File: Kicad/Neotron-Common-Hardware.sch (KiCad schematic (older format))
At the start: 17 parts, among them J101 Neotron-Expansion-Slot, J102 Neotron-Expansion-Slot, J103 Neotron-Expansion-Slot, J104 Neotron-Expansion-Slot, U101 Neotron-CPU

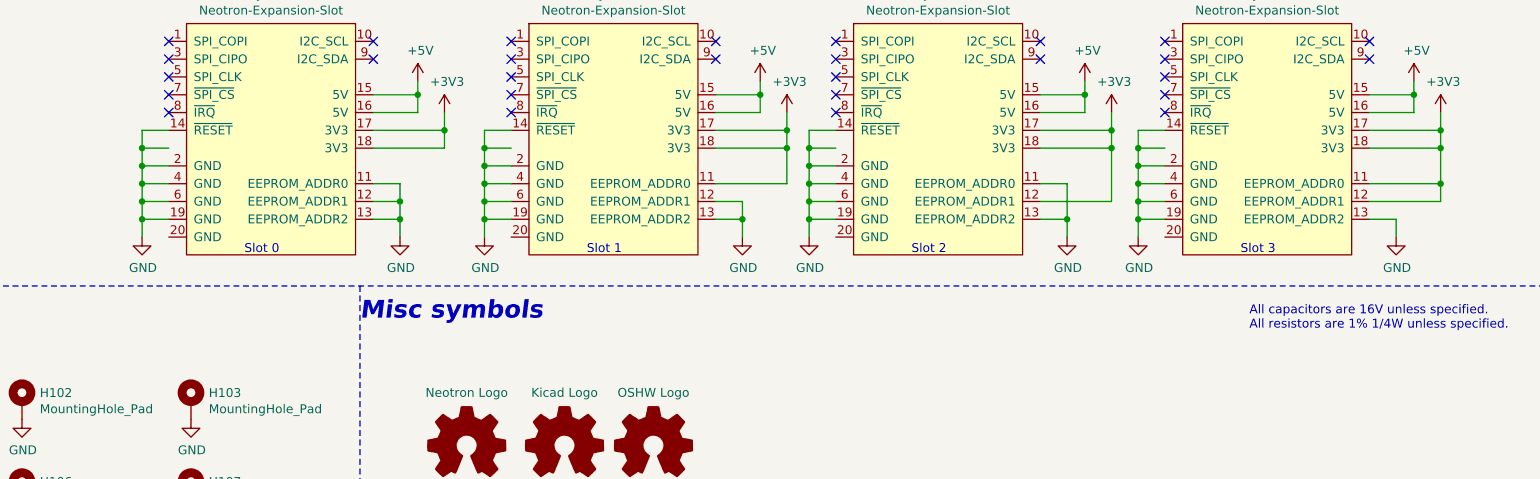
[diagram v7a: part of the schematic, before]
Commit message: Rejigged expansion socket, and added pinout to README.
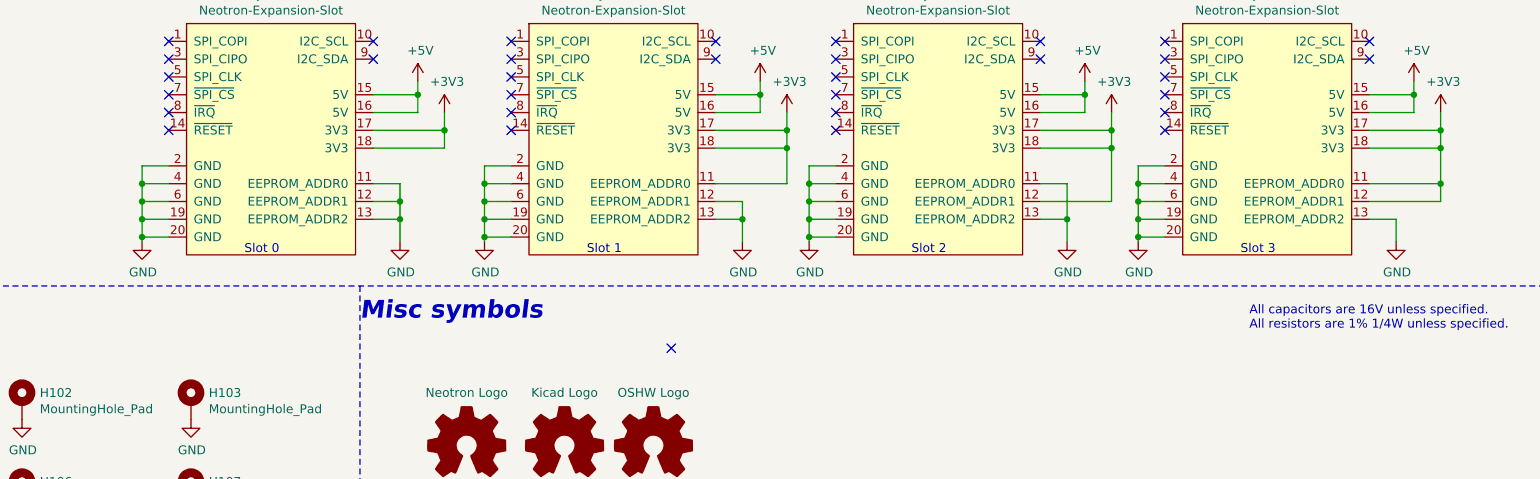
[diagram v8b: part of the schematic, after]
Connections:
- wire segments 128 -> 120
- no-connect marks 120 -> 125
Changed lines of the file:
@@
 L power:GND #PWR0118
 U 1 1 5FED032B
-P 3225 5475
-F 0 "#PWR0118" H 3225 5225 50  0001 C CNN
-F 1 "GND" H 3230 5302 50  0000 C CNN
-F 2 "" H 3225 5475 50  0001 C CNN
-F 3 "" H 3225 5475 50  0001 C CNN
-	1    3225 5475
-	1    0    0    -1
-$EndComp
-Wire Wire Line
-	3375 4875 3225 4875
-Wire Wire Line
-	3375 4975 3225 4975
-Wire Wire Line
-	3225 4875 3225 4975
-Connection ~ 3225 4975
-Wire Wire Line
-	3225 4975 3225 5075
+P 3225 5500
+F 0 "#PWR0118" H 3225 5250 50  0001 C CNN
+F 1 "GND" H 3230 5327 50  0000 C CNN
+F 2 "" H 3225 5500 50  0001 C CNN
+F 3 "" H 3225 5500 50  0001 C CNN
+	1    3225 5500
+	1    0    0    -1
+$EndComp
 Wire Wire Line
 	3375 5075 3225 5075
-Connection ~ 3225 5075
 Wire Wire Line
 	3225 5075 3225 5175
@@
 L power:GND #PWR0119
 U 1 1 5FED378B
-P 4675 5475
-F 0 "#PWR0119" H 4675 5225 50  0001 C CNN
-F 1 "GND" H 4680 5302 50  0000 C CNN
-F 2 "" H 4675 5475 50  0001 C CNN
-F 3 "" H 4675 5475 50  0001 C CNN
-	1    4675 5475
+P 4675 5500
+F 0 "#PWR0119" H 4675 5250 50  0001 C CNN
+F 1 "GND" H 4680 5327 50  0000 C CNN
+F 2 "" H 4675 5500 50  0001 C CNN
+F 3 "" H 4675 5500 50  0001 C CNN
+	1    4675 5500
 	1    0    0    -1
 $EndComp
@@
 	4525 5375 4675 5375
 Wire Wire Line
-	4675 5375 4675 5475
+	4675 5375 4675 5500
 Wire Wire Line
 	4525 5275 4675 5275
@@
 L power:GND #PWR0122
 U 1 1 5FEDE866
-P 5150 5475
-F 0 "#PWR0122" H 5150 5225 50  0001 C CNN
-F 1 "GND" H 5155 5302 50  0000 C CNN
-F 2 "" H 5150 5475 50  0001 C CNN
-F 3 "" H 5150 5475 50  0001 C CNN
-	1    5150 5475
-	1    0    0    -1
-$EndComp
-Wire Wire Line
-	5300 4875 5150 4875
-Wire Wire Line
-	5300 4975 5150 4975
-Wire Wire Line
-	5150 4875 5150 4975
-Connection ~ 5150 4975
-Wire Wire Line
-	5150 4975 5150 5075
+P 5150 5500
+F 0 "#PWR0122" H 5150 5250 50  0001 C CNN
+F 1 "GND" H 5155 5327 50  0000 C CNN
+F 2 "" H 5150 5500 50  0001 C CNN
+F 3 "" H 5150 5500 50  0001 C CNN
+	1    5150 5500
+	1    0    0    -1
+$EndComp
 Wire Wire Line
 	5300 5075 5150 5075
-Connection ~ 5150 5075
 Wire Wire Line
 	5150 5075 5150 5175
@@
 L power:GND #PWR0123
 U 1 1 5FEDE881
-P 6600 5475
-F 0 "#PWR0123" H 6600 5225 50  0001 C CNN
-F 1 "GND" H 6605 5302 50  0000 C CNN
-F 2 "" H 6600 5475 50  0001 C CNN
-F 3 "" H 6600 5475 50  0001 C CNN
-	1    6600 5475
+P 6600 5500
+F 0 "#PWR0123" H 6600 5250 50  0001 C CNN
+F 1 "GND" H 6605 5327 50  0000 C CNN
+F 2 "" H 6600 5500 50  0001 C CNN
+F 3 "" H 6600 5500 50  0001 C CNN
+	1    6600 5500
 	1    0    0    -1
 $EndComp
@@
 	6450 5375 6600 5375
 Wire Wire Line
-	6600 5375 6600 5475
+	6600 5375 6600 5500
 Wire Wire Line
 	6450 5275 6600 5275
@@
 L power:GND #PWR0126
 U 1 1 5FEED11A
-P 6975 5475
-F 0 "#PWR0126" H 6975 5225 50  0001 C CNN
-F 1 "GND" H 6980 5302 50  0000 C CNN
-F 2 "" H 6975 5475 50  0001 C CNN
-F 3 "" H 6975 5475 50  0001 C CNN
-	1    6975 5475
-	1    0    0    -1
-$EndComp
-Wire Wire Line
-	7125 4875 6975 4875
-Wire Wire Line
-	7125 4975 6975 4975
-Wire Wire Line
-	6975 4875 6975 4975
-Connection ~ 6975 4975
-Wire Wire Line
-	6975 4975 6975 5075
+P 6975 5500
+F 0 "#PWR0126" H 6975 5250 50  0001 C CNN
+F 1 "GND" H 6980 5327 50  0000 C CNN
+F 2 "" H 6975 5500 50  0001 C CNN
+F 3 "" H 6975 5500 50  0001 C CNN
+	1    6975 5500
+	1    0    0    -1
+$EndComp
 Wire Wire Line
 	7125 5075 6975 5075
-Connection ~ 6975 5075
 Wire Wire Line
 	6975 5075 6975 5175
@@
 L power:GND #PWR0129
 U 1 1 5FF20385
-P 8425 5475
-F 0 "#PWR0129" H 8425 5225 50  0001 C CNN
-F 1 "GND" H 8430 5302 50  0000 C CNN
-F 2 "" H 8425 5475 50  0001 C CNN
-F 3 "" H 8425 5475 50  0001 C CNN
-	1    8425 5475
+P 8425 5500
+F 0 "#PWR0129" H 8425 5250 50  0001 C CNN
+F 1 "GND" H 8430 5327 50  0000 C CNN
+F 2 "" H 8425 5500 50  0001 C CNN
+F 3 "" H 8425 5500 50  0001 C CNN
+	1    8425 5500
 	1    0    0    -1
 $EndComp
@@
 Connection ~ 8425 5375
 Wire Wire Line
-	8425 5375 8425 5475
+	8425 5375 8425 5500
 Wire Wire Line
 	8275 5275 8675 5275
@@
 L power:GND #PWR0130
 U 1 1 5FF3FC0D
-P 8825 5475
-F 0 "#PWR0130" H 8825 5225 50  0001 C CNN
-F 1 "GND" H 8830 5302 50  0000 C CNN
-F 2 "" H 8825 5475 50  0001 C CNN
-F 3 "" H 8825 5475 50  0001 C CNN
-	1    8825 5475
-	1    0    0    -1
-$EndComp
-Wire Wire Line
-	8975 4875 8825 4875
-Wire Wire Line
-	8975 4975 8825 4975
-Wire Wire Line
-	8825 4875 8825 4975
-Connection ~ 8825 4975
-Wire Wire Line
-	8825 4975 8825 5075
+P 8825 5500
+F 0 "#PWR0130" H 8825 5250 50  0001 C CNN
+F 1 "GND" H 8830 5327 50  0000 C CNN
+F 2 "" H 8825 5500 50  0001 C CNN
+F 3 "" H 8825 5500 50  0001 C CNN
+	1    8825 5500
+	1    0    0    -1
+$EndComp
 Wire Wire Line
 	8975 5075 8825 5075
-Connection ~ 8825 5075
 Wire Wire Line
 	8825 5075 8825 5175
@@
 L power:GND #PWR0133
 U 1 1 5FF3FC4F
-P 10275 5475
-F 0 "#PWR0133" H 10275 5225 50  0001 C CNN
-F 1 "GND" H 10280 5302 50  0000 C CNN
-F 2 "" H 10275 5475 50  0001 C CNN
-F 3 "" H 10275 5475 50  0001 C CNN
-	1    10275 5475
+P 10275 5500
+F 0 "#PWR0133" H 10275 5250 50  0001 C CNN
+F 1 "GND" H 10280 5327 50  0000 C CNN
+F 2 "" H 10275 5500 50  0001 C CNN
+F 3 "" H 10275 5500 50  0001 C CNN
+	1    10275 5500
 	1    0    0    -1
 $EndComp
@@
 	10125 5375 10275 5375
 Wire Wire Line
-	10275 5375 10275 5475
+	10275 5375 10275 5500
 Wire Wire Line
 	10125 5275 10525 5275
@@
 Wire Wire Line
 	10525 5175 10525 5275
+Wire Wire Line
+	3375 5475 3225 5475
+Connection ~ 3225 5475
+Wire Wire Line
+	3225 5475 3225 5500
+Wire Wire Line
+	5300 5475 5150 5475
+Connection ~ 5150 5475
+Wire Wire Line
+	5150 5475 5150 5500
+Wire Wire Line
+	8975 5475 8825 5475
+Connection ~ 8825 5475
+Wire Wire Line
+	8825 5475 8825 5500
+Wire Wire Line
+	7125 5475 6975 5475
+Connection ~ 6975 5475
+Wire Wire Line
+	6975 5475 6975 5500
+NoConn ~ 8975 4875
+NoConn ~ 7125 4875
+NoConn ~ 5300 4875
+NoConn ~ 3375 4875
+NoConn ~ 6200 6100
 $EndSCHEMATC
